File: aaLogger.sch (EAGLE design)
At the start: 64 parts, among them J1 ICSP, Q1 IRLML6244TR, U1 MCP1640C, U2 ATmega328P-AU, U3 DS3232, U4 M24M02, U5 M24M02, Y1 8MHz

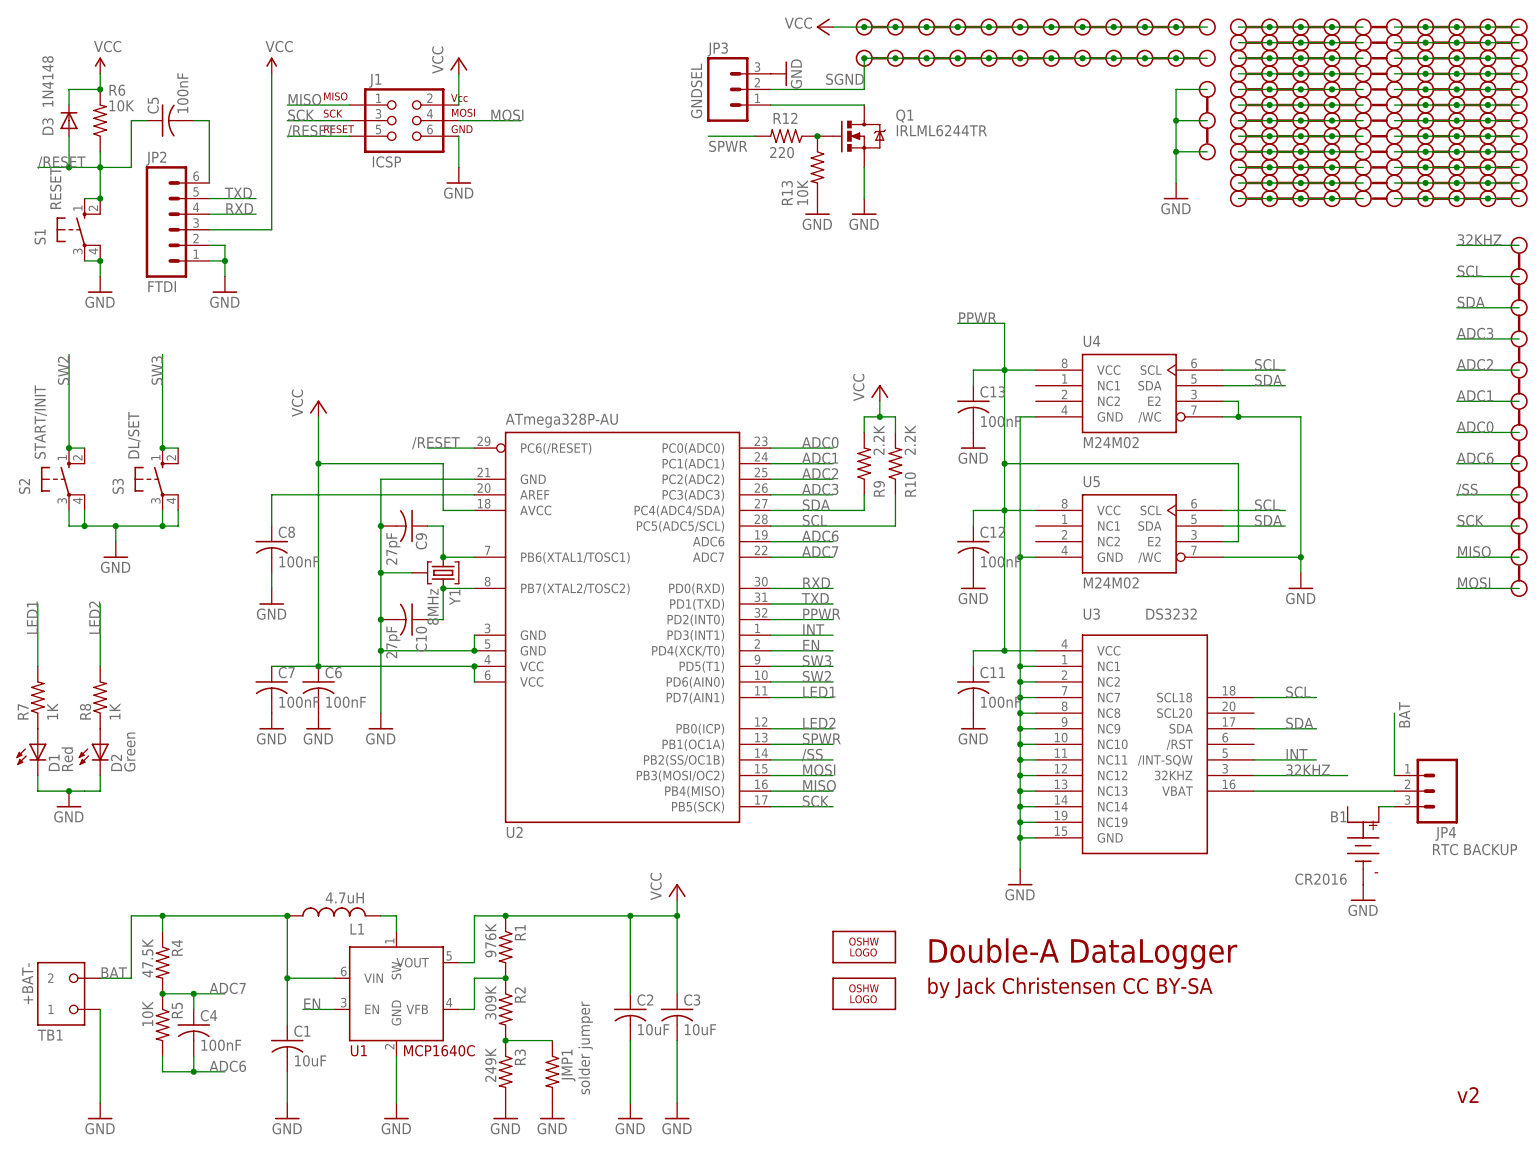
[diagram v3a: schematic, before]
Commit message: Rename resistors. Tweak schematic layout, titles. Put github URL on bottom of board.
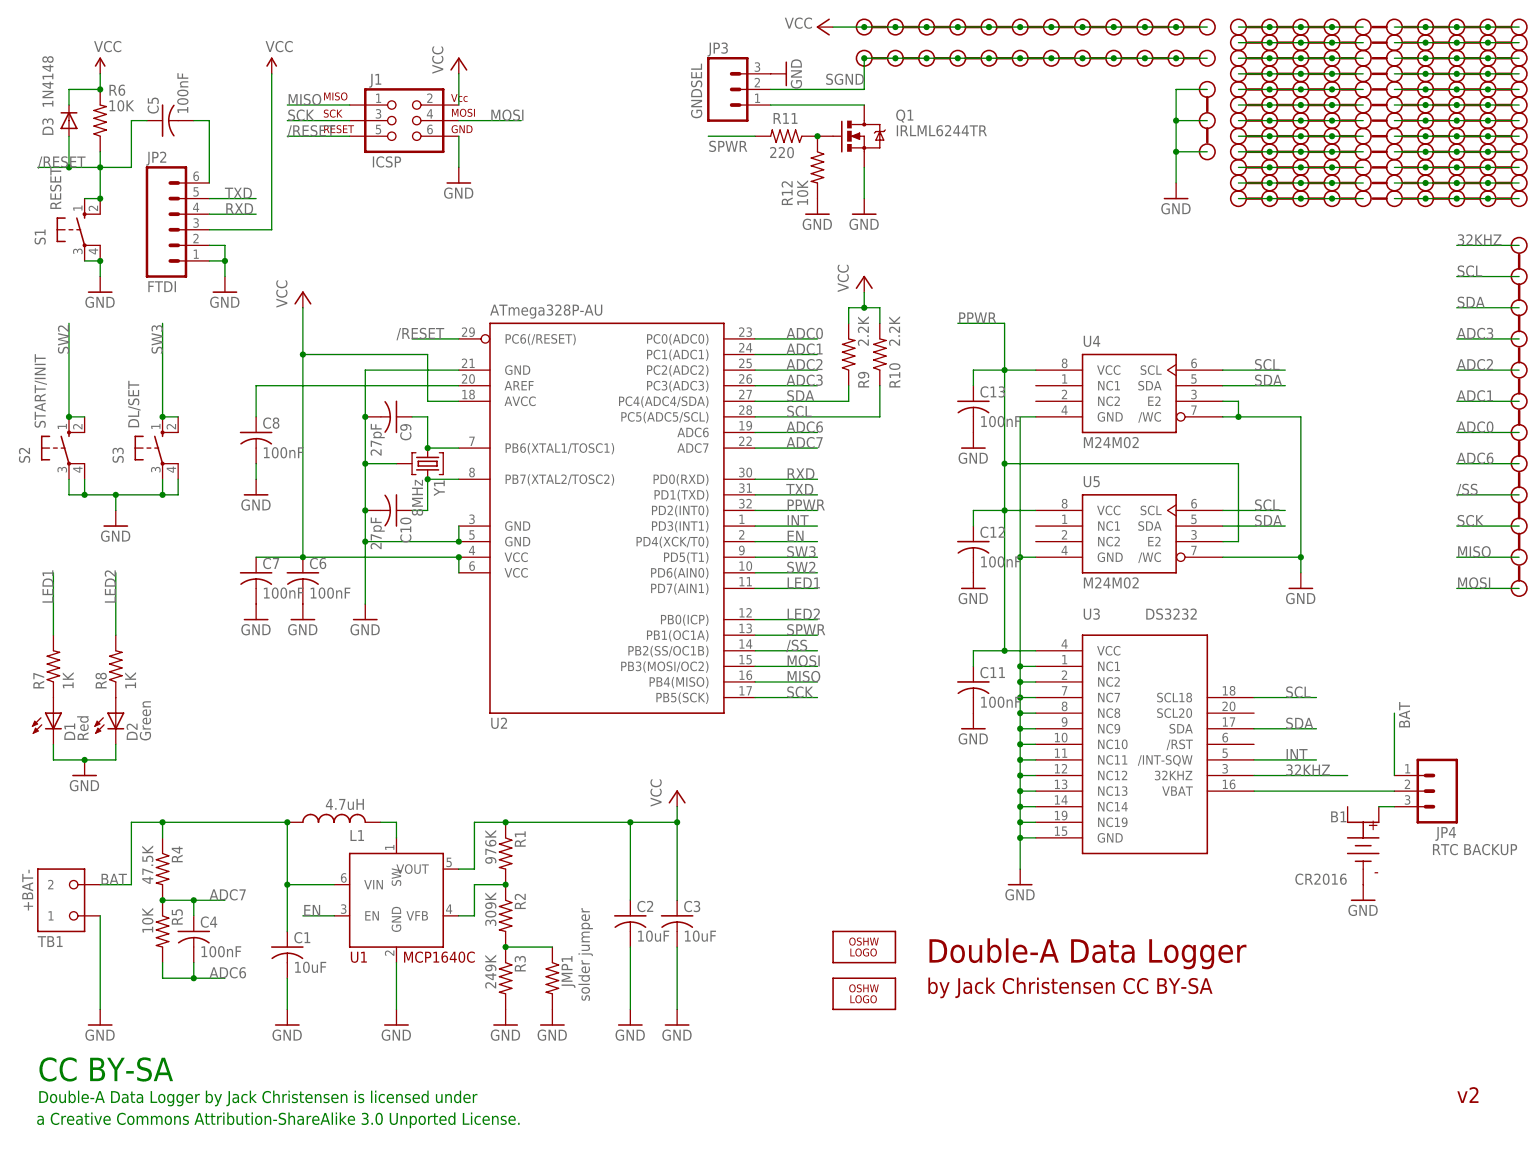
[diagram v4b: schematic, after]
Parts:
- removed R13: 10K, _jc:R-US_M0805
- added R11: 220, _jc:R-US_M0805
- R12: value 220 -> 10K
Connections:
- net GND: now also R12.2; no longer R13.2
- net N$24: now also R11.1; no longer R13.1
- net SPWR: now also R11.2; no longer R12.2
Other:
- note added: "CC BY-SA"
- note added: "Double-A Data Logger"
- note added: "Double-A Data Logger by Jack Christensen is licensed under"
- note added: "a Creative Commons Attribution-ShareAlike 3.0 Unported License."
- note removed: "Double-A DataLogger"
- moved on the sheet: C1, C10, C2, C3, C4, C6, C7, C8, C9, D1, D2, JMP1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
